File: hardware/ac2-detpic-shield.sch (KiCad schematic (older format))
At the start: 2 parts

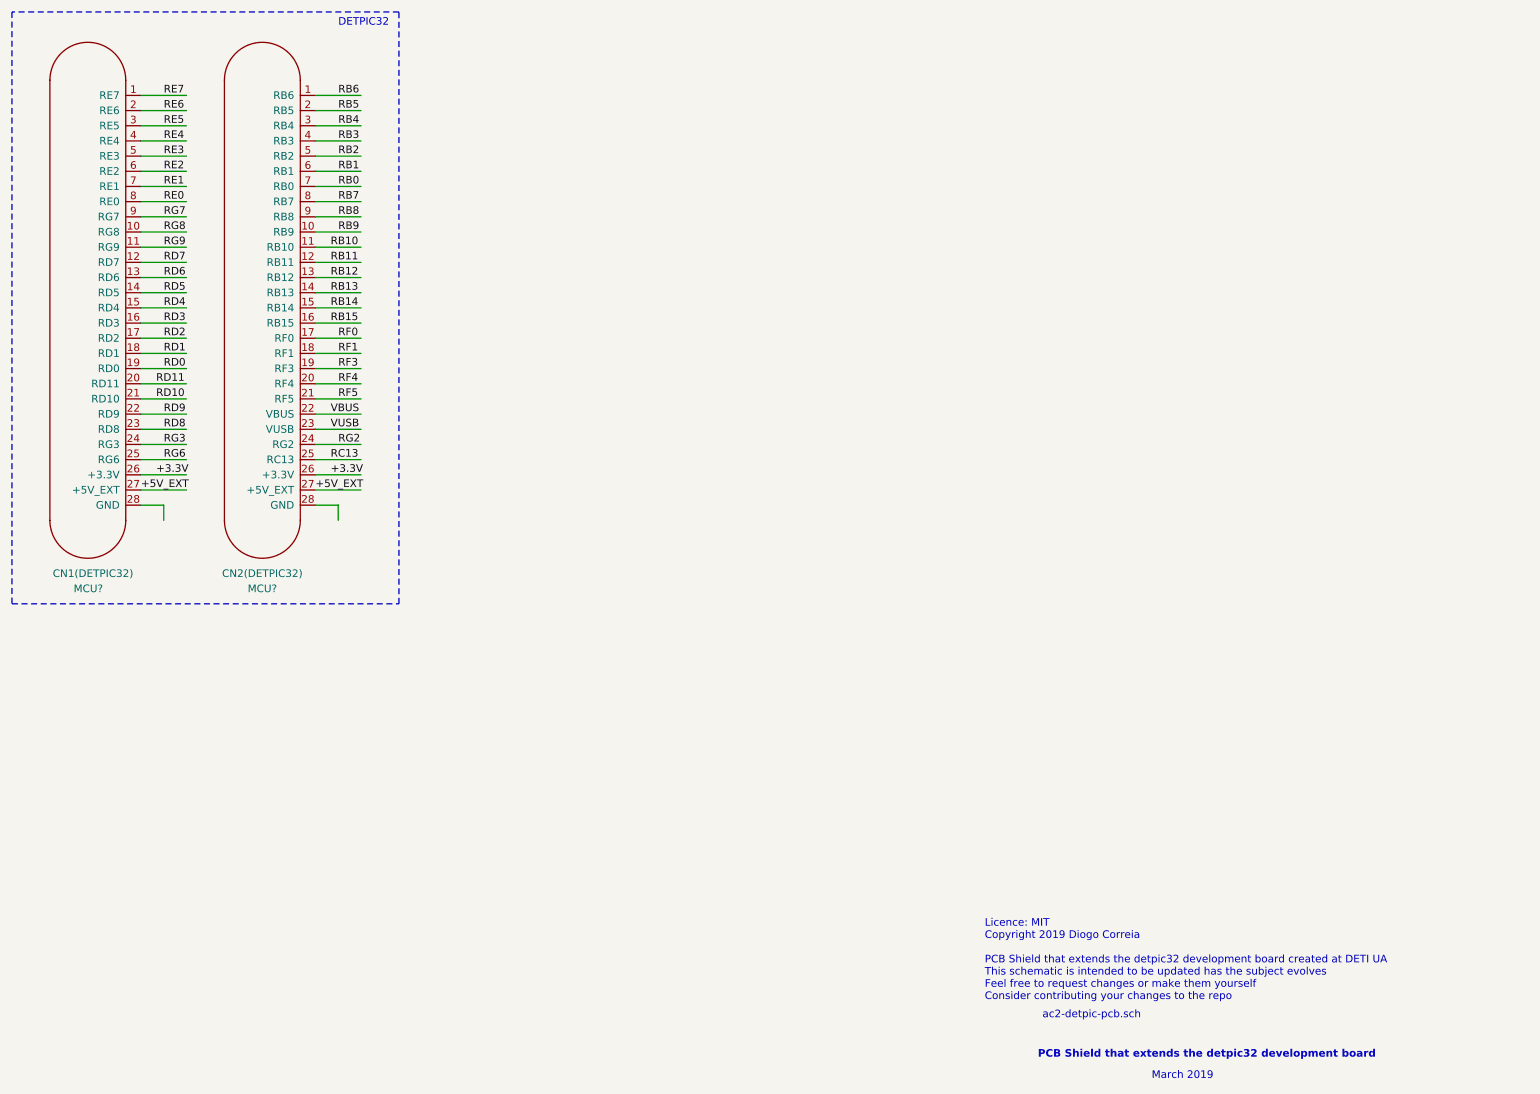
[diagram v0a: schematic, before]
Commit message: reformulation of library handle
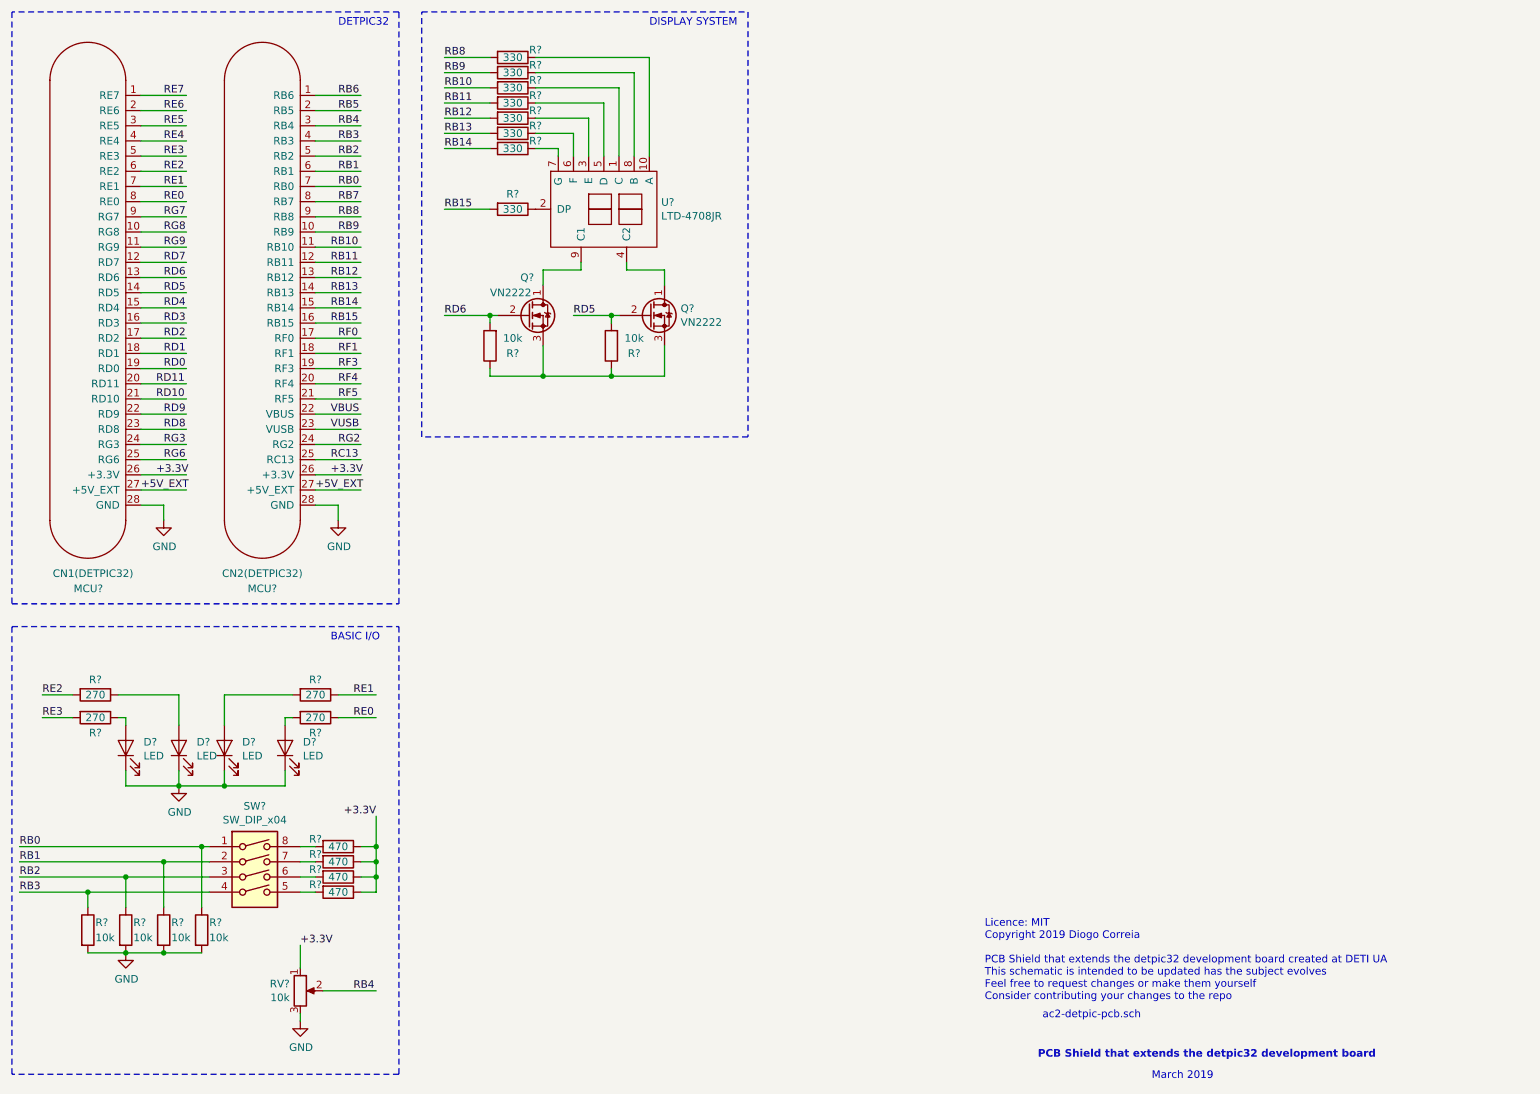
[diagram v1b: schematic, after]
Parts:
- added D? (x4): LED, symbol Device:LED
- added Q? (x2): VN2222, symbol Device:Q_NMOS_DGS
- added R? (x4): 470, symbol Device:R
- added R? (x6): 10k, symbol Device:R
- added R? (x4): 270, symbol Device:R
- added R? (x8): 330, symbol Device:R
- added RV?: 10k, symbol Device:R_POT
- added SW?: SW_DIP_x04, symbol Switch:SW_DIP_x04
- added U?: LTD-4708JR, symbol ac2-detpic-shield:LTD-4708JR
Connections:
- net labels added: GND
- wire segments 58 -> 148
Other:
- note added: "BASIC I/O"
- note added: "DISPLAY SYSTEM"

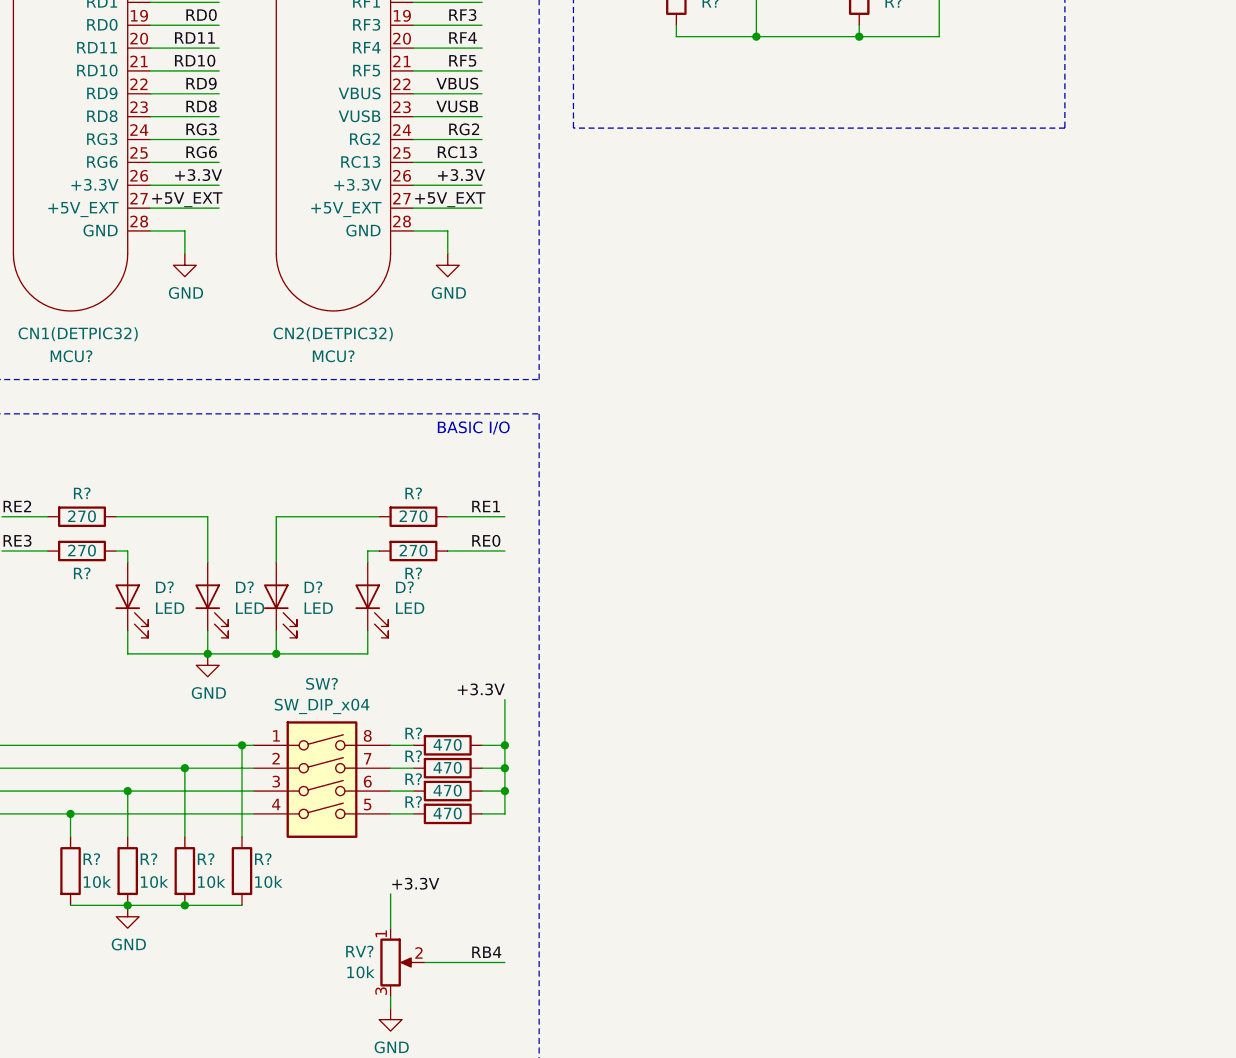
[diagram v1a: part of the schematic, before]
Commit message: added eeprom module
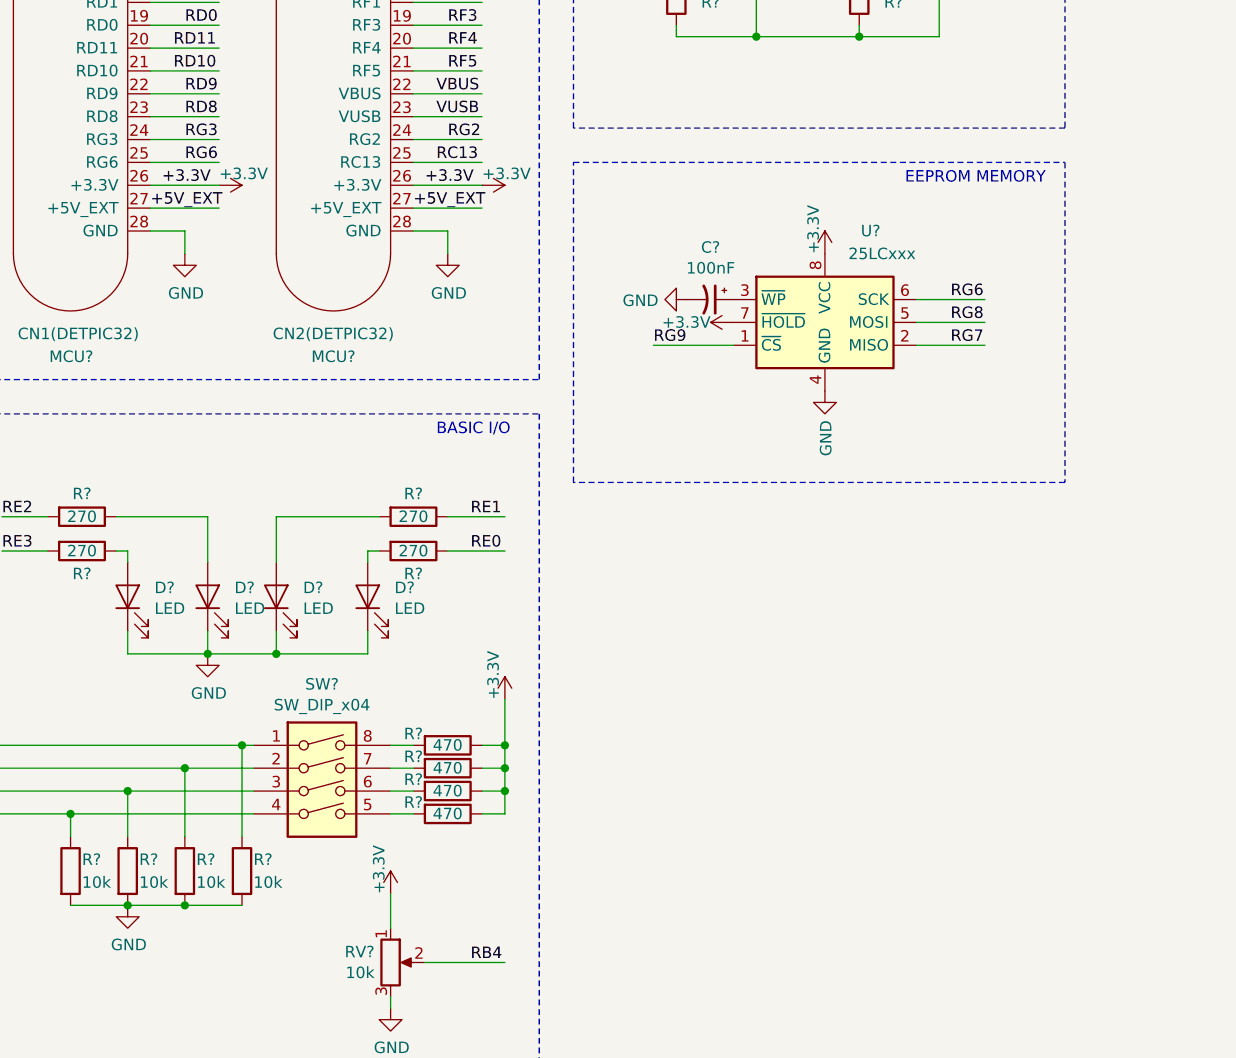
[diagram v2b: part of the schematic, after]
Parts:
- added C?: 100nF, symbol Device:CP1_Small
- added U?: 25LCxxx, symbol Memory_EEPROM:25LCxxx
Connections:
- wire segments 148 -> 152
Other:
- note added: "EEPROM MEMORY"
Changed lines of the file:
@@
 Text Label 1600 3550 0    50   ~ 0
 RG6
-Text Label 1550 3650 0    50   ~ 0
+Text Label 1500 3650 0    50   ~ 0
 +3.3V
 Text Label 1450 3750 0    50   ~ 0
@@
 Text Label 2700 3550 0    50   ~ 0
 RC13
-Text Label 2700 3650 0    50   ~ 0
+Text Label 2650 3650 0    50   ~ 0
 +3.3V
 Text Label 2600 3750 0    50   ~ 0
@@
 Text Label 650  6400 0    50   ~ 0
 RB3
-Text Label 3000 5900 2    50   ~ 0
-+3.3V
 Wire Wire Line
 	2500 7250 2500 7200
@@
 Wire Wire Line
 	2500 6900 2500 6750
-Text Label 2500 6750 0    50   ~ 0
-+3.3V
 Text Label 2850 7050 0    50   ~ 0
 RB4
@@
 	0    1    1    0
 $EndComp
+$Comp
+L Memory_EEPROM:25LCxxx U?
+U 1 1 5C985584
+P 4400 4250
+F 0 "U?" H 4600 4650 50  0000 C CNN
+F 1 "25LCxxx" H 4650 4550 50  0000 C CNN
+F 2 "" H 4400 4250 50  0001 C CNN
+F 3 "http://ww1.microchip.com/downloads/en/DeviceDoc/21832H.pdf" H 4400 4250 50  0001 C CNN
+	1    4400 4250
+	1    0    0    -1
+$EndComp
+$Comp
+L power:+3.3V #PWR?
+U 1 1 5C98EACC
+P 1750 3650
+F 0 "#PWR?" H 1750 3500 50  0001 C CNN
+F 1 "+3.3V" V 1700 3650 50  0000 L CNN
+F 2 "" H 1750 3650 50  0001 C CNN
+F 3 "" H 1750 3650 50  0001 C CNN
+	1    1750 3650
+	0    1    1    0
+$EndComp
+$Comp
+L power:+3.3V #PWR?
+U 1 1 5C990D4A
+P 2900 3650
+F 0 "#PWR?" H 2900 3500 50  0001 C CNN
+F 1 "+3.3V" V 2850 3650 50  0000 L CNN
+F 2 "" H 2900 3650 50  0001 C CNN
+F 3 "" H 2900 3650 50  0001 C CNN
+	1    2900 3650
+	0    1    1    0
+$EndComp
+$Comp
+L power:+3.3V #PWR?
+U 1 1 5C9974F8
+P 3000 5900
+F 0 "#PWR?" H 3000 5750 50  0001 C CNN
+F 1 "+3.3V" V 2950 5900 50  0000 L CNN
+F 2 "" H 3000 5900 50  0001 C CNN
+F 3 "" H 3000 5900 50  0001 C CNN
+	1    3000 5900
+	1    0    0    -1
+$EndComp
+$Comp
+L power:+3.3V #PWR?
+U 1 1 5C99DCA2
+P 2500 6750
+F 0 "#PWR?" H 2500 6600 50  0001 C CNN
+F 1 "+3.3V" V 2450 6750 50  0000 L CNN
+F 2 "" H 2500 6750 50  0001 C CNN
+F 3 "" H 2500 6750 50  0001 C CNN
+	1    2500 6750
+	1    0    0    -1
+$EndComp
+$Comp
+L power:+3.3V #PWR?
+U 1 1 5C9B8AC8
+P 4400 3950
+F 0 "#PWR?" H 4400 3800 50  0001 C CNN
+F 1 "+3.3V" V 4350 3950 50  0000 L CNN
+F 2 "" H 4400 3950 50  0001 C CNN
+F 3 "" H 4400 3950 50  0001 C CNN
+	1    4400 3950
+	1    0    0    -1
+$EndComp
+$Comp
+L power:+3.3V #PWR?
+U 1 1 5C9CE3A0
+P 4000 4250
+F 0 "#PWR?" H 4000 4100 50  0001 C CNN
+F 1 "+3.3V" V 4000 4350 50  0000 L CNN
+F 2 "" H 4000 4250 50  0001 C CNN
+F 3 "" H 4000 4250 50  0001 C CNN
+	1    4000 4250
+	0    -1   -1   0
+$EndComp
+$Comp
+L Device:CP1_Small C?
+U 1 1 5C9D838E
+P 3900 4150
+F 0 "C?" V 3672 4150 50  0000 C CNN
+F 1 "100nF" V 3763 4150 50  0000 C CNN
+F 2 "" H 3900 4150 50  0001 C CNN
+F 3 "~" H 3900 4150 50  0001 C CNN
+	1    3900 4150
+	0    1    1    0
+$EndComp
+$Comp
+L power:GND #PWR?
+U 1 1 5C9D9A74
+P 3800 4150
+F 0 "#PWR?" H 3800 3900 50  0001 C CNN
+F 1 "GND" V 3805 4022 50  0000 R CNN
+F 2 "" H 3800 4150 50  0001 C CNN
+F 3 "" H 3800 4150 50  0001 C CNN
+	1    3800 4150
+	0    1    1    0
+$EndComp
+Wire Wire Line
+	4000 4350 3650 4350
+Text Label 3650 4350 0    50   ~ 0
+RG9
+$Comp
+L power:GND #PWR?
+U 1 1 5C9E2479
+P 4400 4550
+F 0 "#PWR?" H 4400 4300 50  0001 C CNN
+F 1 "GND" V 4405 4422 50  0000 R CNN
+F 2 "" H 4400 4550 50  0001 C CNN
+F 3 "" H 4400 4550 50  0001 C CNN
+	1    4400 4550
+	1    0    0    -1
+$EndComp
+Wire Wire Line
+	4800 4250 5100 4250
+Wire Wire Line
+	4800 4150 5100 4150
+Wire Wire Line
+	4800 4350 5100 4350
+Text Label 4950 4150 0    50   ~ 0
+RG6
+Text Label 4950 4250 0    50   ~ 0
+RG8
+Text Label 4950 4350 0    50   ~ 0
+RG7
+Wire Notes Line
+	3300 3550 5450 3550
+Wire Notes Line
+	5450 3550 5450 4950
+Wire Notes Line
+	5450 4950 3300 4950
+Wire Notes Line
+	3300 4950 3300 3550
+Text Notes 4750 3650 0    50   ~ 0
+EEPROM MEMORY
 $EndSCHEMATC

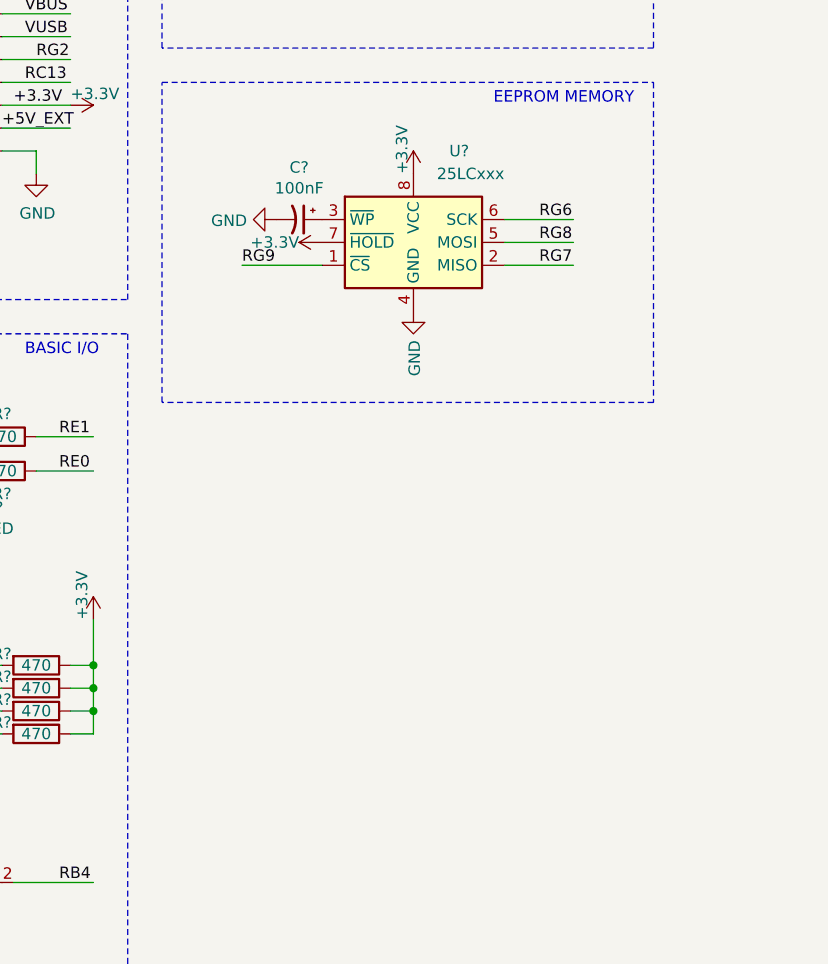
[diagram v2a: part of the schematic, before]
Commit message: added temperature sensor module
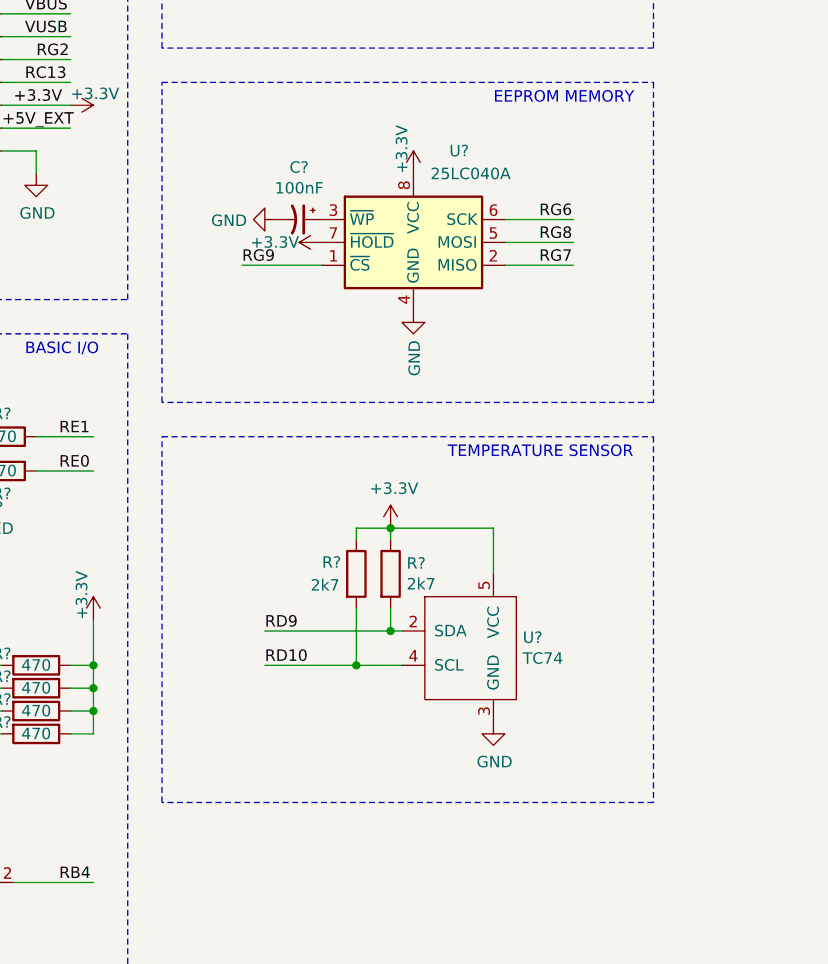
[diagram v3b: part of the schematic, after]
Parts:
- added R? (x2): 2k7, symbol Device:R
- added U?: TC74, symbol ac2-detpic-shield:TC74
- U?: value 25LCxxx -> 25LC040A
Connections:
- wire segments 152 -> 163
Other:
- note added: "TEMPERATURE SENSOR"
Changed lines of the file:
@@
 P 4400 4250
 F 0 "U?" H 4600 4650 50  0000 C CNN
-F 1 "25LCxxx" H 4650 4550 50  0000 C CNN
+F 1 "25LC040A" H 4650 4550 50  0000 C CNN
 F 2 "" H 4400 4250 50  0001 C CNN
 F 3 "http://ww1.microchip.com/downloads/en/DeviceDoc/21832H.pdf" H 4400 4250 50  0001 C CNN
@@
 Text Notes 4750 3650 0    50   ~ 0
 EEPROM MEMORY
+$Comp
+L ac2-detpic-shield:TC74 U?
+U 1 1 5CA20DAE
+P 4750 6050
+F 0 "U?" H 4878 6121 50  0000 L CNN
+F 1 "TC74" H 4878 6030 50  0000 L CNN
+F 2 "" H 4750 6050 50  0001 C CNN
+F 3 "" H 4750 6050 50  0001 C CNN
+	1    4750 6050
+	1    0    0    -1
+$EndComp
+$Comp
+L Device:R R?
+U 1 1 5CA22052
+P 4300 5700
+F 0 "R?" H 4370 5746 50  0000 L CNN
+F 1 "2k7" H 4370 5655 50  0000 L CNN
+F 2 "" V 4230 5700 50  0001 C CNN
+F 3 "~" H 4300 5700 50  0001 C CNN
+	1    4300 5700
+	1    0    0    -1
+$EndComp
+$Comp
+L Device:R R?
+U 1 1 5CA24853
+P 4150 5700
+F 0 "R?" H 4000 5750 50  0000 L CNN
+F 1 "2k7" H 3950 5650 50  0000 L CNN
+F 2 "" V 4080 5700 50  0001 C CNN
+F 3 "~" H 4150 5700 50  0001 C CNN
+	1    4150 5700
+	1    0    0    -1
+$EndComp
+$Comp
+L power:+3.3V #PWR?
+U 1 1 5CA2B8E8
+P 4300 5500
+F 0 "#PWR?" H 4300 5350 50  0001 C CNN
+F 1 "+3.3V" H 4315 5673 50  0000 C CNN
+F 2 "" H 4300 5500 50  0001 C CNN
+F 3 "" H 4300 5500 50  0001 C CNN
+	1    4300 5500
+	1    0    0    -1
+$EndComp
+$Comp
+L power:GND #PWR?
+U 1 1 5CA2D9CF
+P 4750 6350
+F 0 "#PWR?" H 4750 6100 50  0001 C CNN
+F 1 "GND" H 4755 6177 50  0000 C CNN
+F 2 "" H 4750 6350 50  0001 C CNN
+F 3 "" H 4750 6350 50  0001 C CNN
+	1    4750 6350
+	1    0    0    -1
+$EndComp
+Wire Wire Line
+	4150 5550 4150 5500
+Wire Wire Line
+	4150 5500 4300 5500
+Wire Wire Line
+	4300 5550 4300 5500
+Connection ~ 4300 5500
+Wire Wire Line
+	4300 5500 4750 5500
+Wire Wire Line
+	4750 5500 4750 5700
+Wire Wire Line
+	4300 5850 4300 5950
+Wire Wire Line
+	4300 5950 4350 5950
+Wire Wire Line
+	4150 5850 4150 6100
+Wire Wire Line
+	4150 6100 4350 6100
+Wire Wire Line
+	4300 5950 3750 5950
+Connection ~ 4300 5950
+Wire Wire Line
+	4150 6100 3750 6100
+Connection ~ 4150 6100
+Text Label 3750 5950 0    50   ~ 0
+RD9
+Text Label 3750 6100 0    50   ~ 0
+RD10
+Wire Notes Line
+	3300 5100 5450 5100
+Wire Notes Line
+	5450 5100 5450 6700
+Wire Notes Line
+	5450 6700 3300 6700
+Wire Notes Line
+	3300 6700 3300 5100
+Text Notes 4550 5200 0    50   ~ 0
+TEMPERATURE SENSOR
 $EndSCHEMATC
